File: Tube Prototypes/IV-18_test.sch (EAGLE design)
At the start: 7 parts

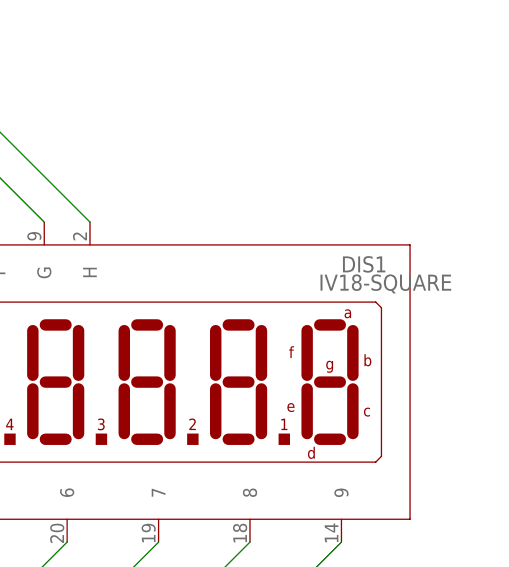
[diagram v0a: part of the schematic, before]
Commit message: new prototype for dual tube board
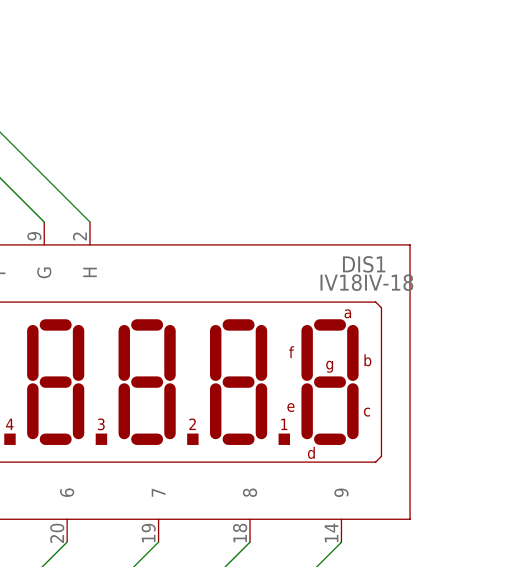
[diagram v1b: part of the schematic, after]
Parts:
- DIS1: value IV18-SQUARE -> IV18IV-18; device iStivi - Tubes:IV18-SQUARE -> iStivi - Tubes:IV18IV-18
- JP1: device iStivi - Header-Connector:M06LONGPADS -> iStivi - Header-Connector:M06SIP
- JP2: device iStivi - Header-Connector:M03LONGPADS -> iStivi - Header-Connector:M03PTH
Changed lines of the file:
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@@
 <?xml version="1.0" encoding="utf-8"?>
 <!DOCTYPE eagle SYSTEM "eagle.dtd">
-<eagle version="6.4">
+<eagle version="6.6.0">
 <drawing>
 <settings>
@@
 <grid distance="0.1" unitdist="inch" unit="inch" style="lines" multiple="1" display="no" altdistance="0.01" altunitdist="inch" altunit="inch"/>
 <layers>
-<layer number="1" name="Top" color="4" fill="1" visible="no" active="no"/>
-<layer number="16" name="Bottom" color="1" fill="1" visible="no" active="no"/>
-<layer number="17" name="Pads" color="2" fill="1" visible="no" active="no"/>
-<layer number="18" name="Vias" color="2" fill="1" visible="no" active="no"/>
-<layer number="19" name="Unrouted" color="6" fill="1" visible="no" active="no"/>
-<layer number="20" name="Dimension" color="15" fill="1" visible="no" active="no"/>
-<layer number="21" name="tPlace" color="7" fill="1" visible="no" active="no"/>
-<layer number="22" name="bPlace" color="7" fill="1" visible="no" active="no"/>
-<layer number="23" name="tOrigins" color="15" fill="1" visible="no" active="no"/>
-<layer number="24" name="bOrigins" color="15" fill="1" visible="no" active="no"/>
-<layer number="25" name="tNames" color="7" fill="1" visible="no" active="no"/>
-<layer number="26" name="bNames" color="7" fill="1" visible="no" active="no"/>
-<layer number="27" name="tValues" color="7" fill="1" visible="no" active="no"/>
-<layer number="28" name="bValues" color="7" fill="1" visible="no" active="no"/>
+<layer number="1" name="Top" color="4" fill="1" visible="yes" active="no"/>
+<layer number="16" name="Bottom" color="1" fill="1" visible="yes" active="no"/>
+<layer number="17" name="Pads" color="2" fill="1" visible="yes" active="no"/>
+<layer number="18" name="Vias" color="2" fill="1" visible="yes" active="no"/>
+<layer number="19" name="Unrouted" color="6" fill="1" visible="yes" active="no"/>
+<layer number="20" name="Dimension" color="15" fill="1" visible="yes" active="no"/>
+<layer number="21" name="tPlace" color="7" fill="1" visible="yes" active="no"/>
+<layer number="22" name="bPlace" color="7" fill="1" visible="yes" active="no"/>
+<layer number="23" name="tOrigins" color="15" fill="1" visible="yes" active="no"/>
+<layer number="24" name="bOrigins" color="15" fill="1" visible="yes" active="no"/>
+<layer number="25" name="tNames" color="7" fill="1" visible="yes" active="no"/>
+<layer number="26" name="bNames" color="7" fill="1" visible="yes" active="no"/>
+<layer number="27" name="tValues" color="7" fill="1" visible="yes" active="no"/>
+<layer number="28" name="bValues" color="7" fill="1" visible="yes" active="no"/>
 <layer number="29" name="tStop" color="7" fill="3" visible="no" active="no"/>
 <layer number="30" name="bStop" color="7" fill="6" visible="no" active="no"/>
@@
 <layer number="35" name="tGlue" color="7" fill="4" visible="no" active="no"/>
 <layer number="36" name="bGlue" color="7" fill="5" visible="no" active="no"/>
-<layer number="37" name="tTest" color="7" fill="1" visible="no" active="no"/>
-<layer number="38" name="bTest" color="7" fill="1" visible="no" active="no"/>
+<layer number="37" name="tTest" color="7" fill="1" visible="yes" active="no"/>
+<layer number="38" name="bTest" color="7" fill="1" visible="yes" active="no"/>
 <layer number="39" name="tKeepout" color="4" fill="11" visible="no" active="no"/>
 <layer number="40" name="bKeepout" color="1" fill="11" visible="no" active="no"/>
@@
 <layer number="44" name="Drills" color="7" fill="1" visible="no" active="no"/>
 <layer number="45" name="Holes" color="7" fill="1" visible="no" active="no"/>
-<layer number="46" name="Milling" color="3" fill="1" visible="no" active="no"/>
-<layer number="47" name="Measures" color="7" fill="1" visible="no" active="no"/>
-<layer number="48" name="Document" color="7" fill="1" visible="no" active="no"/>
-<layer number="49" name="Reference" color="7" fill="1" visible="no" active="no"/>
-<layer number="50" name="dxf" color="7" fill="1" visible="no" active="no"/>
-<layer number="51" name="tDocu" color="7" fill="1" visible="no" active="no"/>
-<layer number="52" name="bDocu" color="7" fill="1" visible="no" active="no"/>
-<layer number="53" name="tGND_GNDA" color="7" fill="9" visible="no" active="no"/>
-<layer number="54" name="bGND_GNDA" color="1" fill="9" visible="no" active="no"/>
-<layer number="56" name="wert" color="7" fill="1" visible="no" active="no"/>
+<layer number="46" name="Milling" color="3" fill="1" visible="yes" active="no"/>
+<layer number="47" name="Measures" color="7" fill="1" visible="yes" active="no"/>
+<layer number="48" name="Document" color="7" fill="1" visible="yes" active="no"/>
+<layer number="49" name="Reference" color="7" fill="1" visible="yes" active="no"/>
+<layer number="50" name="dxf" color="7" fill="1" visible="yes" active="no"/>
+<layer number="51" name="tDocu" color="7" fill="1" visible="yes" active="no"/>
+<layer number="52" name="bDocu" color="7" fill="1" visible="yes" active="no"/>
+<layer number="53" name="tGND_GNDA" color="7" fill="9" visible="yes" active="no"/>
+<layer number="54" name="bGND_GNDA" color="1" fill="9" visible="yes" active="no"/>
+<layer number="56" name="wert" color="7" fill="1" visible="yes" active="no"/>
 <layer number="91" name="Nets" color="2" fill="1" visible="yes" active="yes"/>
 <layer number="92" name="Busses" color="1" fill="1" visible="yes" active="yes"/>
@@
 <part name="P+2" library="iStivi - Supply" deviceset="VCC" device=""/>
 <part name="R1" library="iStivi - RCLD" deviceset="R-US_" device="0207/10" value="56R"/>
-<part name="JP1" library="iStivi - Header-Connector" deviceset="M06" device="LONGPADS"/>
+<part name="JP1" library="iStivi - Header-Connector" deviceset="M06" device="SIP"/>
 <part name="GND2" library="iStivi - Supply" deviceset="GND" device=""/>
 <part name="GND3" library="iStivi - Supply" deviceset="GND" device=""/>
 <part name="C1" library="iStivi - RCLD" deviceset="CPOL-US" device="E2-5" value="10uF"/>
 <part name="C2" library="iStivi - RCLD" deviceset="CPOL-US" device="E2-5" value="100nF"/>
-<part name="JP2" library="iStivi - Header-Connector" deviceset="M03" device="LONGPADS"/>
+<part name="JP2" library="iStivi - Header-Connector" deviceset="M03" device="PTH"/>
 <part name="P+3" library="iStivi - Supply" deviceset="VCC" device=""/>
 <part name="U$3" library="iStivi - Supply" deviceset="VBB" device=""/>
 <part name="GND4" library="iStivi - Supply" deviceset="GND" device=""/>
-<part name="DIS1" library="iStivi - Tubes" deviceset="IV18" device="-SQUARE"/>
+<part name="DIS1" library="iStivi - Tubes" deviceset="IV18" device="IV-18" value="IV18IV-18"/>
 </parts>
 <sheets>
